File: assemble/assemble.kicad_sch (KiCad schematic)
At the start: 110 parts, among them J1 Conn_02x04_Odd_Even, SW1 SW_Push, SW10 SW_Push, SW11 SW_Push, SW12 SW_Push, SW13 SW_Push, SW14 SW_Push, SW15 SW_Push, SW16 SW_Push, SW17 SW_Push, SW18 SW_Push, SW19 SW_Push, SW2 SW_Push, SW20 SW_Push, SW21 SW_Push, SW22 SW_Push, SW23 SW_Push, SW24 SW_Push, SW25 SW_Push, SW26 SW_Push, SW27 SW_Push, SW28 SW_Push, SW29 SW_Push, SW3 SW_Push, SW30 SW_Push, SW31 SW_Push, SW32 SW_Push, SW33 SW_Push, SW34 SW_Push, SW35 SW_Push, SW36 SW_Push, SW37 SW_Push, SW38 SW_Push, SW39 SW_Push, SW4 SW_Push, SW40 SW_Push, SW41 SW_Push, SW42 SW_Push, SW43 SW_SPDT, SW44 SW_SPDT, SW45 RotaryEncoder_Switch, SW5 SW_Push, SW6 SW_Push, SW7 SW_Push, SW8 SW_Push, SW9 SW_Push, U1 XIAO-nRF52840-SMD, U2 XIAO-nRF52840-SMD

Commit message: feat: finish implement PCB
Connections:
- net BAT+L: no longer U1.3 (P0.28_A2_D2)
- net BAT+R: no longer U2.1 (P0.02_A0_D0)
- net PIN1R: now also U2.1 (P0.02_A0_D0); no longer U2.2 (P0.03_A1_D1)
- net PIN2R: now also U2.2 (P0.03_A1_D1); no longer U2.4 (P0.29_A3_D3)
- net PIN3R: now also U2.4 (P0.29_A3_D3); no longer U2.5 (P0.04_A4_D4_SDA)
- net PIN4R: now also U2.5 (P0.04_A4_D4_SDA); no longer U2.6 (P0.05_A5_D5_SCL)
- net PIN5R: now also U2.6 (P0.05_A5_D5_SCL); no longer U2.7 (P1.11_D6_TX)
- net PIN6R: now also U2.7 (P1.11_D6_TX); no longer U2.8 (P1.12_D7_RX)
- net PIN7R: now also U2.8 (P1.12_D7_RX); no longer U2.18 (NFC2)
- no-connect marks 20 -> 22

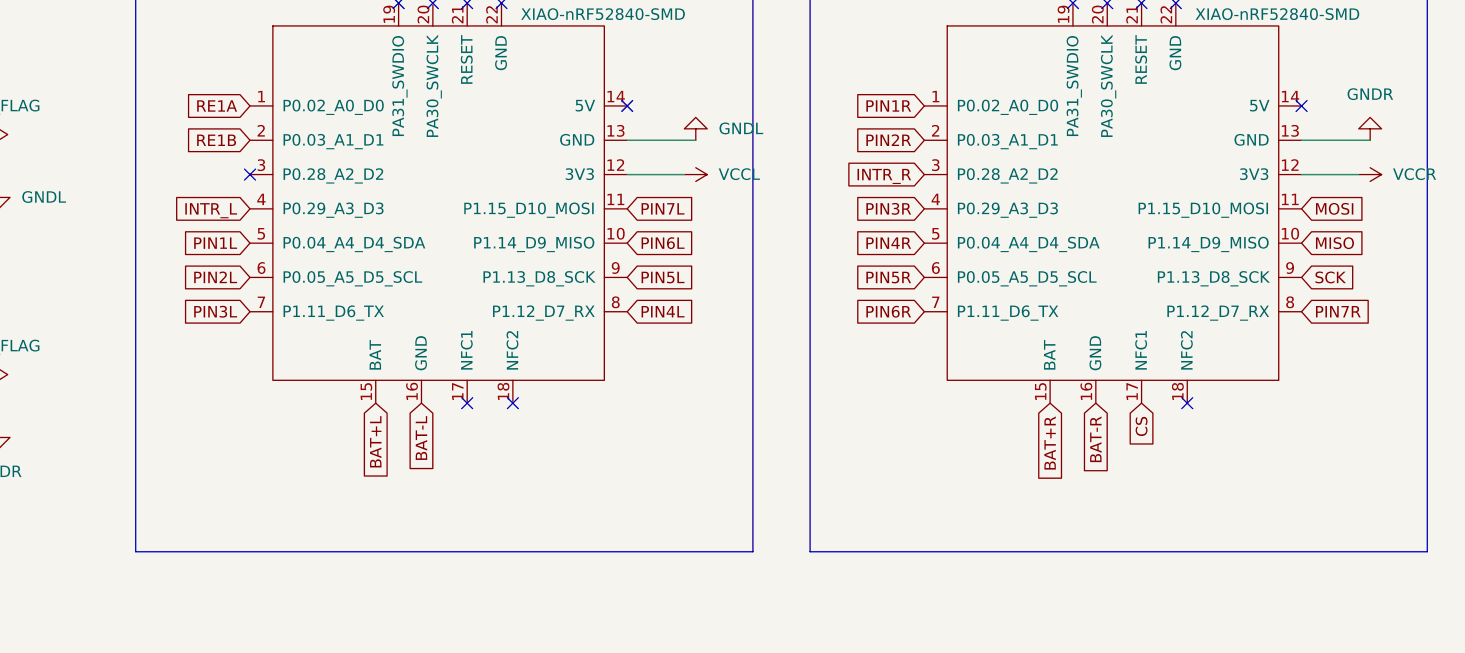
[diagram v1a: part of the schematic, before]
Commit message: fix: change position
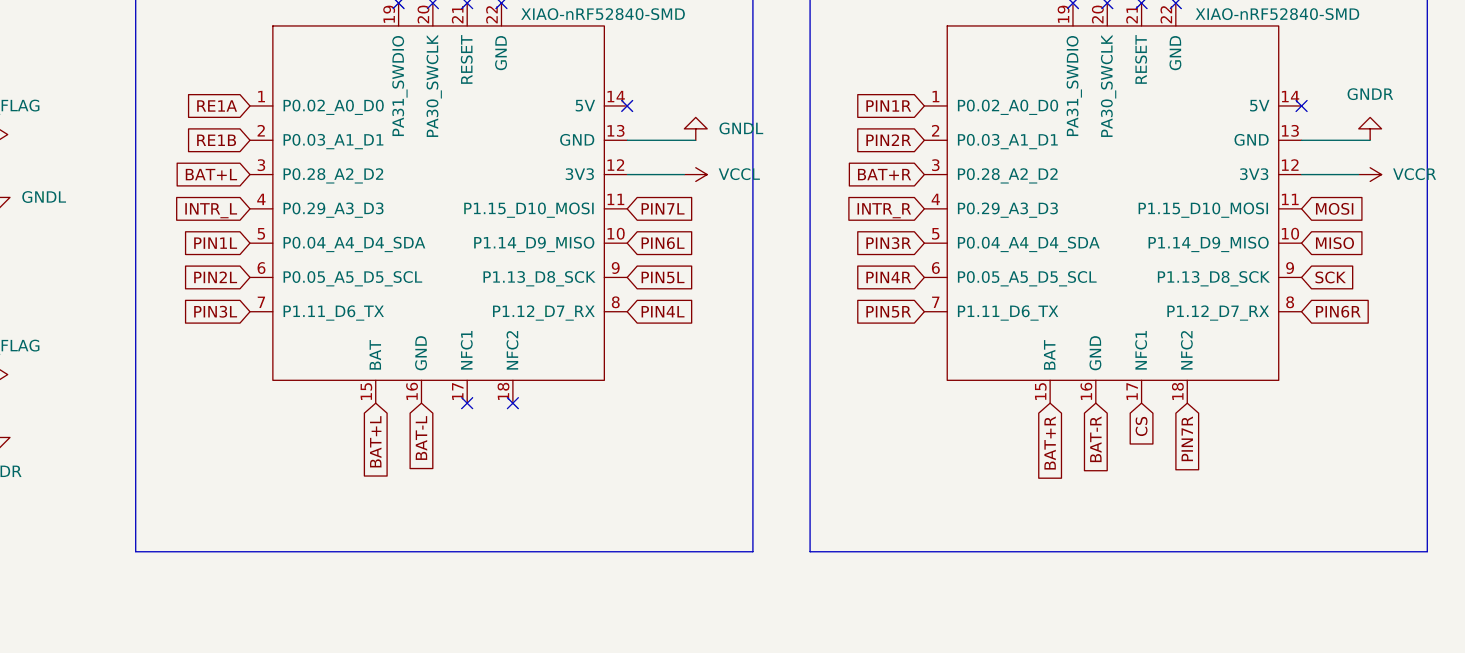
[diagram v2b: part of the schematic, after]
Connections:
- net BAT+L: now also U1.3 (P0.28_A2_D2)
- net BAT+R: now also U2.3 (P0.28_A2_D2)
- net INTR_R: now also U2.4 (P0.29_A3_D3); no longer U2.3 (P0.28_A2_D2)
- net PIN3R: now also U2.5 (P0.04_A4_D4_SDA); no longer U2.4 (P0.29_A3_D3)
- net PIN4R: now also U2.6 (P0.05_A5_D5_SCL); no longer U2.5 (P0.04_A4_D4_SDA)
- net PIN5R: now also U2.7 (P1.11_D6_TX); no longer U2.6 (P0.05_A5_D5_SCL)
- net PIN6R: now also U2.8 (P1.12_D7_RX); no longer U2.7 (P1.11_D6_TX)
- net PIN7R: now also U2.18 (NFC2); no longer U2.8 (P1.12_D7_RX)
- no-connect marks 22 -> 20

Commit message: feat: change case and re-wired
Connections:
- net BAT+L: no longer U1.3 (P0.28_A2_D2)
- net BAT+R: no longer U2.3 (P0.28_A2_D2)
- net B+L: now reaches AE-XCL102D333CR-G2.6 (IN), BT2.1 (+)
- net B+L: now also U1.3 (P0.28_A2_D2)
- net B+R: now reaches AE-XCL102D333CR-G1.6 (IN), BT1.1 (+)
- net B+R: now also U2.3 (P0.28_A2_D2)
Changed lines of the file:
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@@
-	(wire
-		(pts
-			(xy 270.51 262.89) (xy 270.51 255.27)
-		)
-		(stroke
-			(width 0)
-			(type default)
-		)
-	)
 	(wire
 		(pts
@@
 	(wire
 		(pts
-			(xy 273.05 224.79) (xy 273.05 217.17)
-		)
-		(stroke
-			(width 0)
-			(type default)
-		)
-	)
-	(wire
-		(pts
 			(xy 123.19 46.99) (xy 127 46.99)
 		)
@@
 		)
 	)
+	(global_label "B+L"
+		(shape input)
+		(at 273.05 224.79 180)
+		(fields_autoplaced yes)
+		(effects
+			(font
+				(size 1.27 1.27)
+			)
+			(justify right)
+		)
+		(property "Intersheetrefs" "${INTERSHEET_REFS}"
+			(at 266.1943 224.79 0)
+			(effects
+				(font
+					(size 1.27 1.27)
+				)
+				(justify right)
+				(hide yes)
+			)
+		)
+	)
 	(global_label "PIN3L"
 		(shape input)
@@
 		)
 	)
+	(global_label "B+L"
+		(shape input)
+		(at 273.05 217.17 0)
+		(fields_autoplaced yes)
+		(effects
+			(font
+				(size 1.27 1.27)
+			)
+			(justify left)
+		)
+		(property "Intersheetrefs" "${INTERSHEET_REFS}"
+			(at 279.9057 217.17 0)
+			(effects
+				(font
+					(size 1.27 1.27)
+				)
+				(justify left)
+				(hide yes)
+			)
+		)
+	)
 	(global_label "PIN5L"
 		(shape input)
@@
 		)
 	)
+	(global_label "B+R"
+		(shape input)
+		(at 270.51 255.27 0)
+		(fields_autoplaced yes)
+		(effects
+			(font
+				(size 1.27 1.27)
+			)
+			(justify left)
+		)
+		(property "Intersheetrefs" "${INTERSHEET_REFS}"
+			(at 277.6076 255.27 0)
+			(effects
+				(font
+					(size 1.27 1.27)
+				)
+				(justify left)
+				(hide yes)
+			)
+		)
+	)
 	(global_label "SCK"
 		(shape input)
@@
 		)
 	)
-	(global_label "BAT+R"
+	(global_label "B+R"
+		(shape input)
+		(at 270.51 262.89 180)
+		(fields_autoplaced yes)
+		(effects
+			(font
+				(size 1.27 1.27)
+			)
+			(justify right)
+		)
+		(property "Intersheetrefs" "${INTERSHEET_REFS}"
+			(at 263.4124 262.89 0)
+			(effects
+				(font
+					(size 1.27 1.27)
+				)
+				(justify right)
+				(hide yes)
+			)
+		)
+	)
+	(global_label "B+R"
 		(shape input)
 		(at 342.9 46.99 180)
@@
 		)
 		(property "Intersheetrefs" "${INTERSHEET_REFS}"
-			(at 333.7462 46.99 0)
+			(at 335.8024 46.99 0)
 			(effects
 				(font
@@
 		)
 	)
-	(global_label "BAT+L"
+	(global_label "B+L"
 		(shape input)
 		(at 267.97 46.99 180)
@@
 		)
 		(property "Intersheetrefs" "${INTERSHEET_REFS}"
-			(at 259.0581 46.99 0)
-			(effects
-				(font
+			(at 261.1143 46.99 0)
+			(effects
+				(font
